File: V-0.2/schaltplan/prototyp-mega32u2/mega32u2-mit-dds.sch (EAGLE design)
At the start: 32 parts, among them X1 PN61729-S

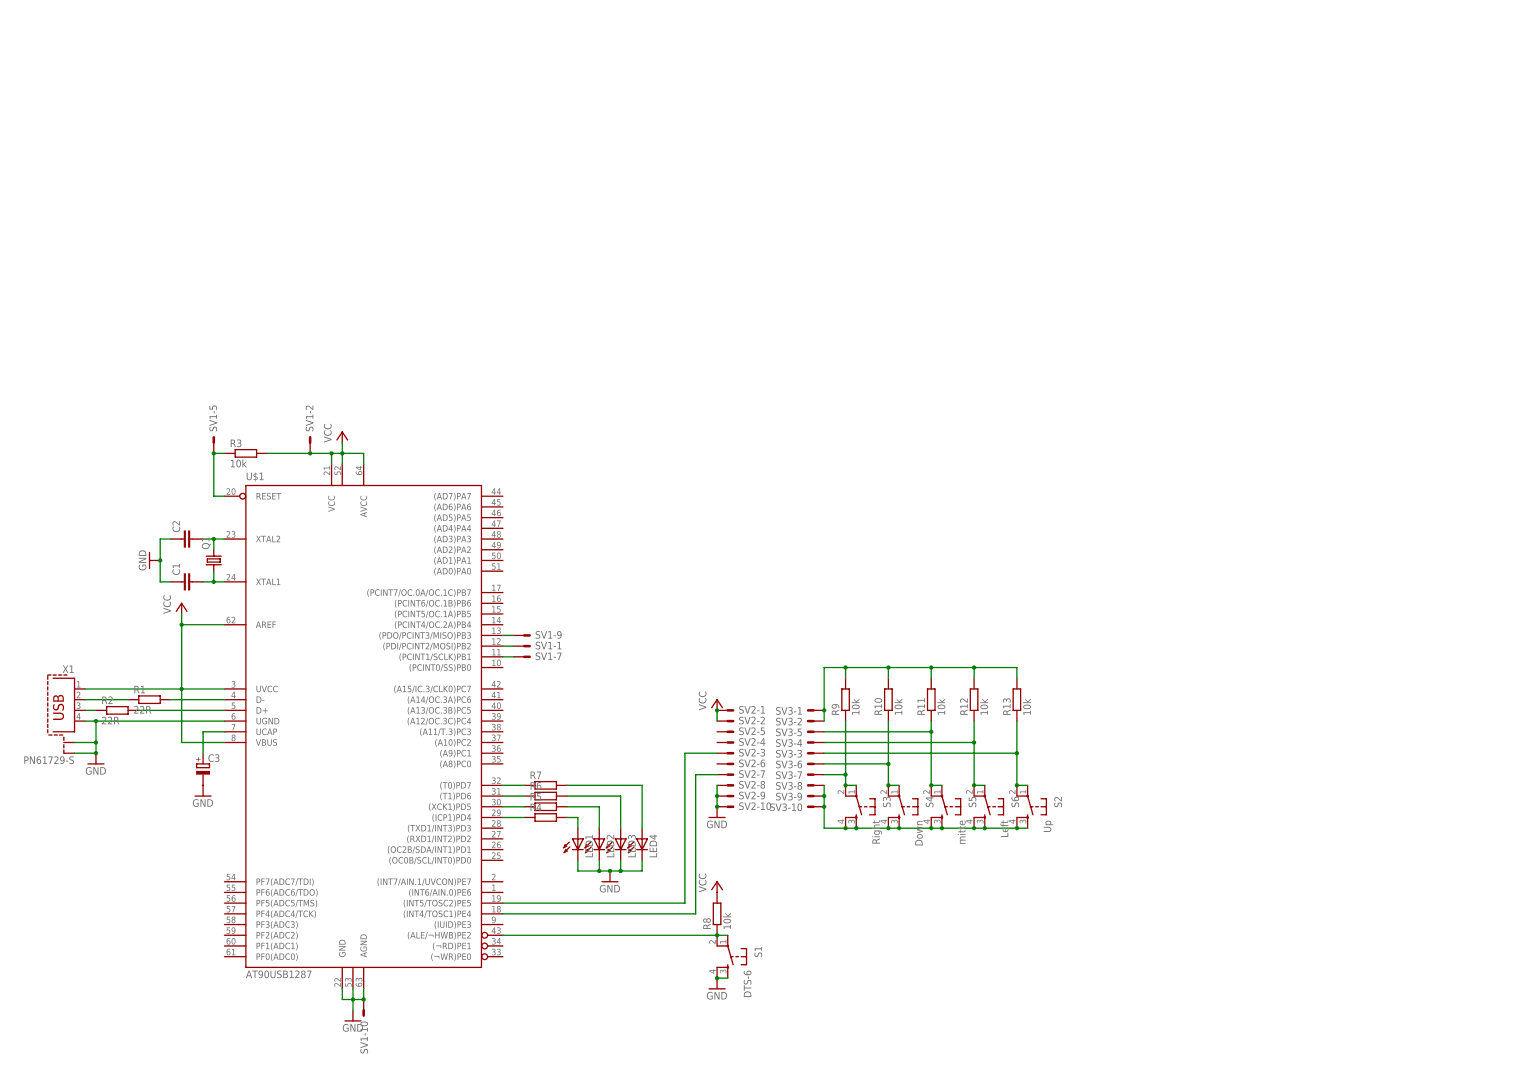
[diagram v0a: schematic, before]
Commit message: removed at90 circuit diagramm, added mega32u2
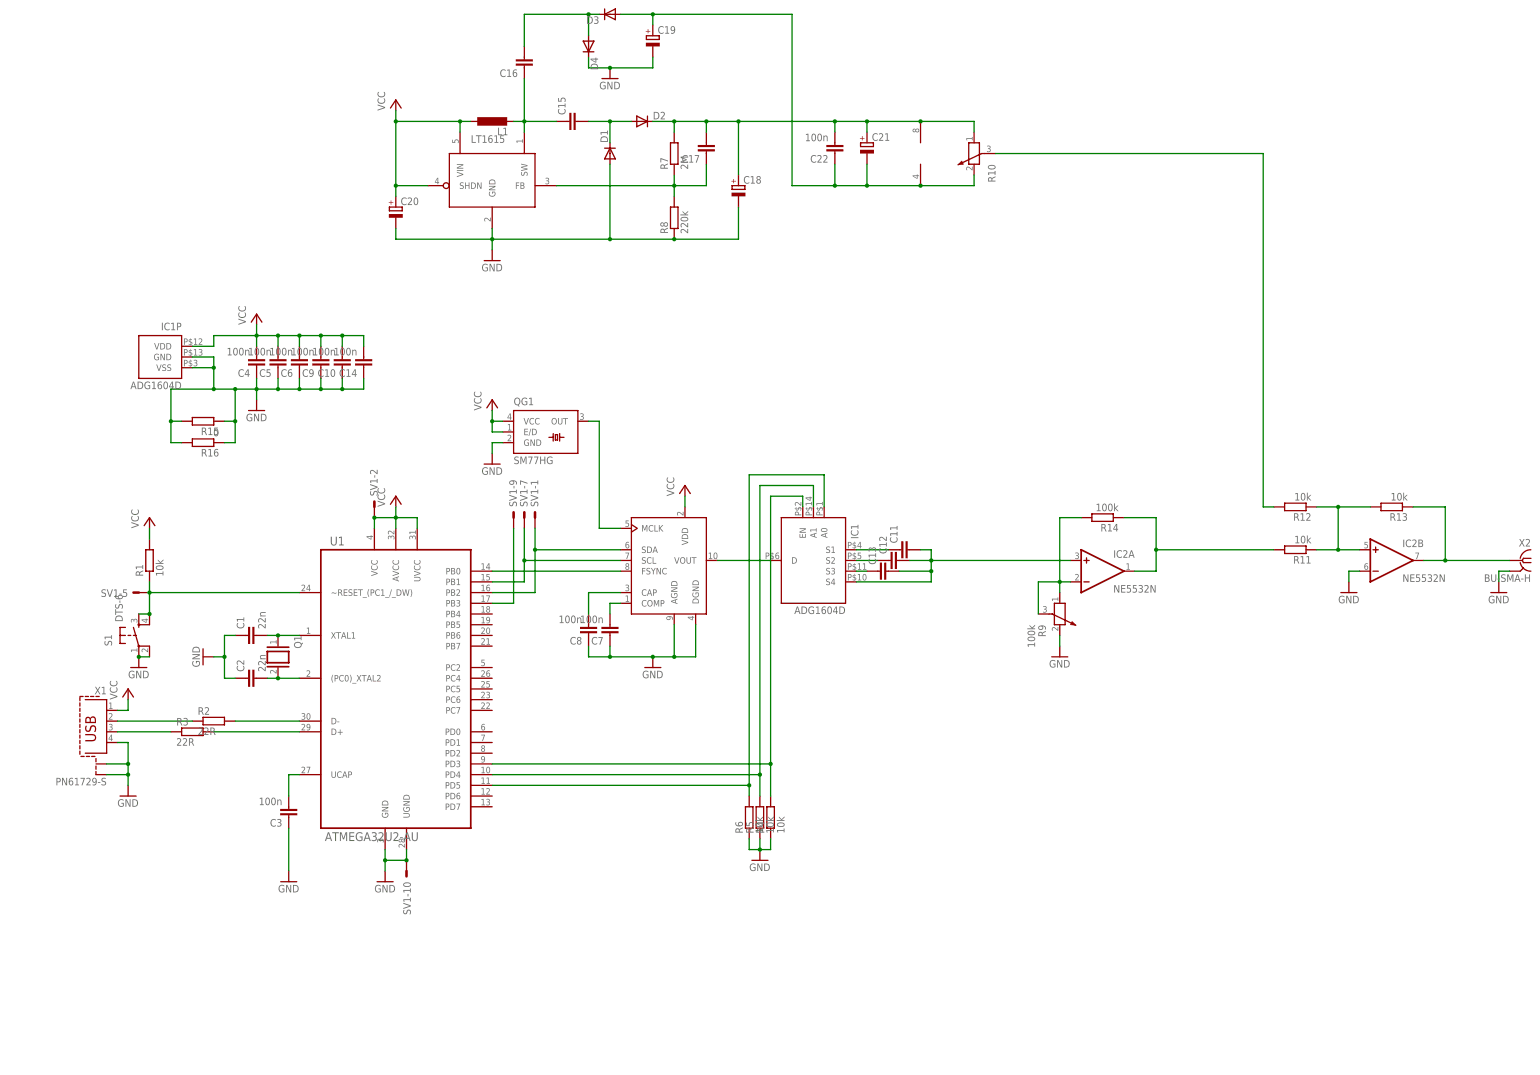
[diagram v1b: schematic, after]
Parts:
- removed LED1, LED2, LED3, LED4: (no value), led:LED3MM
- removed S2: Up, switch-tact:DTS-6
- removed S3: Right, switch-tact:DTS-6
- removed S4: Down, switch-tact:DTS-6
- removed S5: mitte, switch-tact:DTS-6
- removed S6: Left, switch-tact:DTS-6
- removed SV2, SV3: (no value), con-harting-ml:ML10E
- added C10, C14, C22, C4, C5, C6, C7, C8, C9: 100n, rcl:C-EUC0603
- added C11, C12, C13: (no value), rcl:C-EU025-024X044
- added C15, C16, C17: (no value), rcl:C-EU025-030X050
- added C18, C19, C20, C21: (no value), rcl:CPOL-EUE2,5-6E
- added D1, D2, D3, D4: 1N4148DO35-7, diode:1N4148DO35-7
- added IC1: ADG1604D, analog-devices:ADG1604D
- added IC2: NE5532N, linear:NE5532N
- added L1: (no value), rcl:L-EU0207/12
- added QG1: SM77HG, crystal:SM77HG
- added R14: 100k, rcl:R-EU_0207/10
- added R15: (no value), rcl:R-EU_M1206
- added R16: 0, rcl:R-EU_M1206
- added U$2: LT1615, linear:LT1615
- added U1: ATMEGA32U2-AU, Atmel-ATMEGA32U2-AU:ATMEGA32U2-AU
- added X2: BU-SMA-H, con-coax:BU-SMA-H
- C1, C2: value (none) -> 22n; device rcl:C-EUC1206K -> rcl:C-EUC1206
- C3: value (none) -> 100n; device rcl:CPOL-EUE2-5 -> rcl:C-EUC0603
- Q1: device crystal:CRYSTALSM77H -> special:XTAL/S
- R1: value 22R -> 10k; device rcl:R-EU_M1206 -> rcl:R-EU_R0603
- R10: value 10k -> (none); device rcl:R-EU_M1206 -> rcl:POTENTIOMETER_PT-10
- R11, R12, R13: device rcl:R-EU_M1206 -> rcl:R-EU_R0603
- R3: value 10k -> 22R; device rcl:R-EU_0207/10 -> rcl:R-EU_M1206
- R4, R5, R6: value (none) -> 10k; device rcl:R-EU_0207/10 -> rcl:R-EU_R0603
- R7: value (none) -> 2M
- R8: value 10k -> 220k; device rcl:R-EU_M1206 -> rcl:R-EU_0207/10
- R9: value 10k -> 100k; device rcl:R-EU_M1206 -> rcl:POTENTIOMETER_PT-10
- U$1: value AT90USB1287 -> AD9833-P; device atmelusb:AT90USB1287 -> analog-devices:AD9833-P
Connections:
- removed net N$28: R11.1, S5.1, S5.2, SV3-5.S
- removed net N$30: R9.1, S3.1, S3.2, SV3-7.S
- new net N$25: C15.1, C16.1, L1.2, U$2.SW
- new net N$26: C16.2, D3.C, D4.A
- new net N$27: C17.1, R7.1, R8.2, U$2.FB
- new net N$33: R10.3, R12.2
- new net N$34: IC2A.-IN, R14.2, R9.1, R9.3
- new net N$35: IC2A.OUT, R11.2, R14.1
- new net N$36: IC2B.OUT, R13.1, X2.1
- net GND: now also C10.1, C14.1, C18.-, C19.-, C20.-, C3.1, C4.1, C5.1, C6.1, C7.1, C8.1, C9.1, D1.A, D4.C, IC1P.GND, IC1P.VSS, IC2B.-IN, QG1.GND, R15.1, R15.2, R16.1, R16.2, R4.1, R5.1, R6.1, R8.1, R9.2, S1.1, S1.2, U$1.DGND, U$2.GND, U1.GND, U1.UGND, X2.2; no longer C3.-, LED1.C, LED2.C, LED3.C, LED4.C, S1.3, S1.4, SV2-10.S, SV2-8.S, SV2-9.S, U$1.GND, U$1.GND1, U$1.UGND
- net N$1: now also C2.2, Q1.2, U1.(PC0)_XTAL2; no longer R1.2, U$1.D-
- net N$10: now also U$1.FSYNC, U1.PB0; no longer R6.1, U$1.(T1)PD6
- net N$11: now also C8.2, U$1.CAP; no longer R3.1, SV1-5.S, U$1.RESET
- net N$12: now also C7.2, U$1.COMP; no longer SV1-9.S, U$1.(PDO/PCINT3/MISO)PB3
- net N$13: now also R3.1, X1.3; no longer SV1-1.S, U$1.(PDI/PCINT2/MOSI)PB2
- net N$14: now also R2.1, X1.2; no longer SV1-7.S, U$1.(PCINT1/SCLK)PB1
- net N$15: now also QG1.OUT, U$1.MCLK; no longer R7.1, U$1.(T0)PD7
- net N$16: now also IC1G$1.D, U$1.VOUT; no longer LED1.A, R4.2
- net N$17: now also C13.1, IC1G$1.S3; no longer LED2.A, R5.2
- net N$18: now also C12.1, IC1G$1.S2; no longer LED3.A, R6.2
- net N$19: now also C11.1, IC1G$1.S1; no longer LED4.A, R7.2
- net N$2: now also C1.2, Q1.1, U1.XTAL1; no longer R2.2, U$1.D+
- net N$20: now also C11.2, C12.2, C13.2, IC1G$1.S4, IC2A.+IN; no longer R8.1, S1.1, S1.2, U$1.(ALE/¬HWB)PE2
- net N$21: now also IC1G$1.EN, R4.2, U1.PD3; no longer R13.1, S2.1, S2.2, SV3-3.S
- net N$22: now also IC1G$1.A1, R5.2, U1.PD4; no longer R12.1, S6.1, S6.2, SV3-4.S
- net N$23: now also IC1G$1.A0, R6.2, U1.PD5; no longer SV2-7.S, U$1.(INT4/TOSC1)PE4
- net N$24: now also C15.2, D1.C, D2.A; no longer SV2-3.S, U$1.(INT5/TOSC2)PE5
- net N$29: now also C17.2, C18.+, C21.+, C22.2, D2.C, IC2P.V+, R7.2; no longer S4.1, S4.2, SV3-6.S
- net N$3: now also SV1-9.S, U1.PB3; no longer R1.1, X1.2
- net N$31: now also C19.+, C21.-, C22.1, D3.A, IC2P.V-, R10.2; no longer S2.3, S2.4, S3.3, S3.4, S4.3, S4.4, S5.3, S5.4, S6.3, S6.4, SV3-10.S, SV3-8.S, SV3-9.S
- net N$32: now also IC2B.+IN, R11.1, R12.1; no longer R10.2, R11.2, R12.2, R9.2, SV3-1.S, SV3-2.S
- net N$4: now also SV1-1.S, U$1.SDA, U1.PB2; no longer R2.1, X1.3
- net N$5: now also R2.2, U1.D-; no longer C2.2, Q1.2, U$1.XTAL2
- net N$6: now also R3.2, U1.D+; no longer C1.2, Q1.1, U$1.XTAL1
- net N$7: now also C3.2, U1.UCAP; no longer R4.1, U$1.(ICP1)PD4
- net N$8: now also R1.1, S1.3, S1.4, SV1-5.S, U1.~RESET_(PC1_/_DW); no longer C3.+, U$1.UCAP
- net N$9: now also SV1-7.S, U$1.SCL, U1.PB1; no longer R5.1, U$1.(XCK1)PD5
- net VCC: now also C10.2, C14.2, C20.+, C4.2, C5.2, C6.2, C9.2, IC1P.VDD, L1.1, QG1.E/D, QG1.VCC, R1.2, U$1.VDD, U$2.SHDN, U$2.VIN, U1.AVCC, U1.UVCC, U1.VCC; no longer R3.2, R8.2, SV2-1.S, SV2-2.S, U$1.AREF, U$1.AVCC, U$1.UVCC, U$1.VBUS, U$1.VCC, U$1.VCC1
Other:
- moved on the sheet: C1, C2, R1, R11, R12, R13, R2, R3, R4, R5, R6, R7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
